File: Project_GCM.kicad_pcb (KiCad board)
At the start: 4 copper layers, 203 x 116 mm, 127 parts, among them J1 PowerSupply, J10 MM1_addressExtension, J11 MM1_receptacle_5530843-2, J12 DEBUG_BUSES, J13 MM1_addressExtension, J2 PP1_receptacle_TE_5-5530843-4, J3 PP1_receptacle_TE_5-5530843-4, J4 PP1_receptacle_TE_5-5530843-4, J5 PP1_receptacle_TE_5-5530843-4, J6 TE_Eurocard_96pole, J7 3-641124-6, J8 MM1_receptacle_5530843-2, J9 Conn_01x02, U1 LM810, U10 74LVC1G74, U11 74AHC1G04, U12 74AHC244, U13 CD74AC161M, U14 CD74AC161M, U15 74AHCT1G04, U16 CD74AC161M, U17 CD74AC161M, U18 74AHC1G04, U19 CD74AC161M, U2 LTC6994xS6-1, U20 CD74AC161M, U21 74AHCT244, U22 74CBTLV16212, U23 74CBTLV16212, U24 74CBTLV16212, U25 74AHC1G32, U26 SN74LV393A, U27 SN74LV393A, U28 CD74AC151, U29 CD74AC151, U3 74AHC1G32, U30 74AHC1G32, U31 CD74AC151, U32 74AHC273, U33 SN74LV393A, U34 SN74LV393A, U35 CD74AC151, U36 CD74AC151, U37 CD74AC151, U38 74AHC1G04, U39 74AHC1G04, U4 74AHC273, U40 74AHC273, U41 74AHC1G04, U42 74AHC273, U43 74AHC273, U44 74AHC273, U5 74AHC1G04, U6 CD74AC238, U7 74AHC138, U8 74AHC244, U9 74AHC244, X1 ECS-2200BX-500

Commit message: Netlist, apply change to board, clean track, #6 #4 #12 #10
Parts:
- removed C51: 10nF, Capacitor_SMD:C_0805_2012Metric
- removed G***: LOGO, QRCode:QRCode
- removed U38, U39: 74AHC1G04, Package_TO_SOT_SMD:SOT-23-5
- added C56: 1uF, Capacitor_SMD:C_0805_2012Metric, B.Cu at (258.0, 54.0)
- C11, C4: footprint Capacitor_SMD:C_1206_3216Metric -> Capacitor_SMD:C_0805_2012Metric
- C2: value 10nF -> 1uF
- C3, C5: value 10nF -> 100nF
- J12: footprint Connector_PinSocket_2.54mm:PinSocket_2x21_P2.54mm_Vertical -> Connector_PinHeader_2.54mm:PinHeader_2x21_P2.54mm_Vertical
- J7: footprint Connector_PinSocket_2.54mm:PinSocket_1x06_P2.54mm_Vertical -> TE_3-641124-6:TE_3-641124-6
- J9: footprint Connector_PinSocket_2.54mm:PinSocket_1x02_P2.54mm_Vertical -> Connector_PinHeader_2.54mm:PinHeader_1x02_P2.54mm_Vertical
- moved C14 14.9 mm to (144.0, 143.0)
- moved C2 14.8 mm to (263.0, 47.0), turned to 180 degrees
- moved C5 9.50 mm to (256.0, 54.0), turned to 90 degrees
- moved R5 7.02 mm to (143.0, 136.0)
- moved J7 7.00 mm to (139.0, 139.5), turned to 0 degrees
- moved C3 5.41 mm to (263.0, 45.0), turned to 180 degrees
- moved C15 3.04 mm to (253.0, 38.0)
- moved J12 2.31 mm to (198.1, 40.6)
- moved R4 1.12 mm to (190.5, 44.5)
- moved J9 1.08 mm to (190.5, 38.1)
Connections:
- C2 pad 1: +12V -> +5V
- U13 pad 2: /AddressCounter/ADDSRC_DELAYED_CLK -> /ADDSRC_CLK
- U14 pad 2: /AddressCounter/ADDSRC_DELAYED_CLK -> /ADDSRC_CLK
- U16 pad 2: /AddressCounter/ADDSRC_DELAYED_CLK -> /ADDSRC_CLK
- U17 pad 2: /AddressCounter/ADDSRC_DELAYED_CLK -> /ADDSRC_CLK
- U19 pad 2: /AddressCounter/ADDSRC_DELAYED_CLK -> /ADDSRC_CLK
- U20 pad 2: /AddressCounter/ADDSRC_DELAYED_CLK -> /ADDSRC_CLK
- U26 pad 3: /ClockGenerator/CLK_50d16MHZ -> /ClockGenerator/CLK_50d2MHZ
- U26 pad 4: /ClockGenerator/CLK_50d8MHZ -> /ClockGenerator/CLK_50d4MHZ
- U26 pad 5: /ClockGenerator/CLK_50d4MHZ -> /ClockGenerator/CLK_50d8MHZ
- U26 pad 6: /ClockGenerator/CLK_50d2MHZ -> /ClockGenerator/CLK_50d16MHZ
- U27 pad 3: /ClockGenerator/CLK_50d4096MHZ -> /ClockGenerator/CLK_50d512MHZ
- U27 pad 4: /ClockGenerator/CLK_50d2048MHZ -> /ClockGenerator/CLK_50d1024MHZ
- U27 pad 5: /ClockGenerator/CLK_50d1024MHZ -> /ClockGenerator/CLK_50d2048MHZ
- U27 pad 6: /ClockGenerator/CLK_50d512MHZ -> /ClockGenerator/CLK_50d4096MHZ
- U33 pad 3: /ClockGenerator/PClockGenerator/CLK_50d16MHZ -> /ClockGenerator/PClockGenerator/CLK_50d2MHZ
- U33 pad 4: /ClockGenerator/PClockGenerator/CLK_50d8MHZ -> /ClockGenerator/PClockGenerator/CLK_50d4MHZ
- U33 pad 5: /ClockGenerator/PClockGenerator/CLK_50d4MHZ -> /ClockGenerator/PClockGenerator/CLK_50d8MHZ
- U33 pad 6: /ClockGenerator/PClockGenerator/CLK_50d2MHZ -> /ClockGenerator/PClockGenerator/CLK_50d16MHZ
- U34 pad 3: /ClockGenerator/PClockGenerator/CLK_50d4096MHZ -> /ClockGenerator/PClockGenerator/CLK_50d512MHZ
- U34 pad 4: /ClockGenerator/PClockGenerator/CLK_50d2048MHZ -> /ClockGenerator/PClockGenerator/CLK_50d1024MHZ
- U34 pad 5: /ClockGenerator/PClockGenerator/CLK_50d1024MHZ -> /ClockGenerator/PClockGenerator/CLK_50d2048MHZ
- U34 pad 6: /ClockGenerator/PClockGenerator/CLK_50d512MHZ -> /ClockGenerator/PClockGenerator/CLK_50d4096MHZ
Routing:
- net GND: track 1447.7 -> 0.00 mm, vias 15 -> 0
- net +5V: track 790.6 -> 0.00 mm, vias 12 -> 0
- net +3V3: track 535.7 -> 0.00 mm, vias 7 -> 0
- net /ClockGenerator/BWRITE1_5: track 330.1 -> 0.00 mm, vias 5 -> 0
- net /ClockGenerator/BWRITE1_0: track 326.7 -> 0.00 mm, vias 6 -> 0
- net /ClockGenerator/BWRITE1_4: track 324.2 -> 0.00 mm, vias 5 -> 0
- net /ClockGenerator/BWRITE1_1: track 309.6 -> 0.00 mm, vias 4 -> 0
- net /ClockGenerator/BWRITE1_2: track 309.0 -> 0.00 mm, vias 4 -> 0
- net /Connector/BWRITE2_4: track 302.5 -> 0.00 mm, vias 4 -> 0
- net /ClockGenerator/BWRITE1_3: track 300.6 -> 0.00 mm, vias 5 -> 0
- net /Connector/BWRITE2_0: track 299.3 -> 0.00 mm, vias 5 -> 0
- net /Connector/BWRITE2_2: track 295.9 -> 0.00 mm, vias 4 -> 0
- net /Connector/BWRITE2_5: track 294.0 -> 0.00 mm, vias 5 -> 0
- net /Connector/BWRITE2_1: track 289.8 -> 0.00 mm, vias 3 -> 0
- net /Connector/BWRITE2_3: track 285.9 -> 0.00 mm, vias 3 -> 0
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
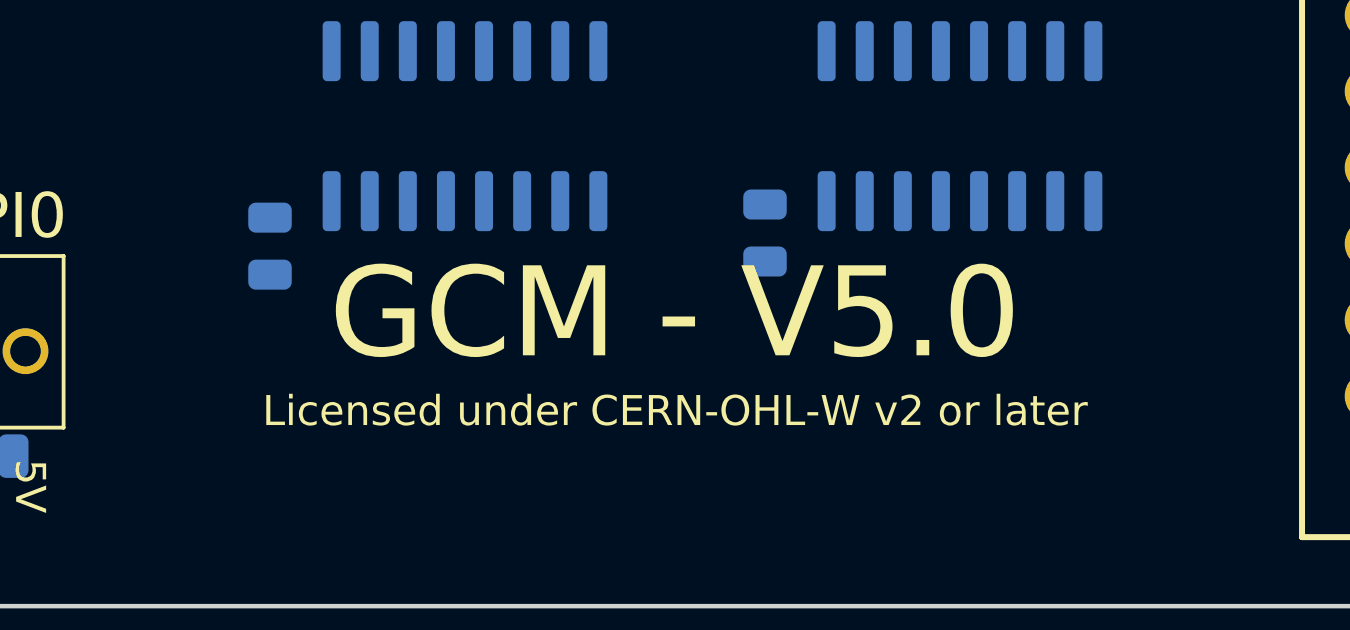
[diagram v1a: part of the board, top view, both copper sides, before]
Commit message: Set version to 5.1, 2021 copyright and date, replace the missing QRcode
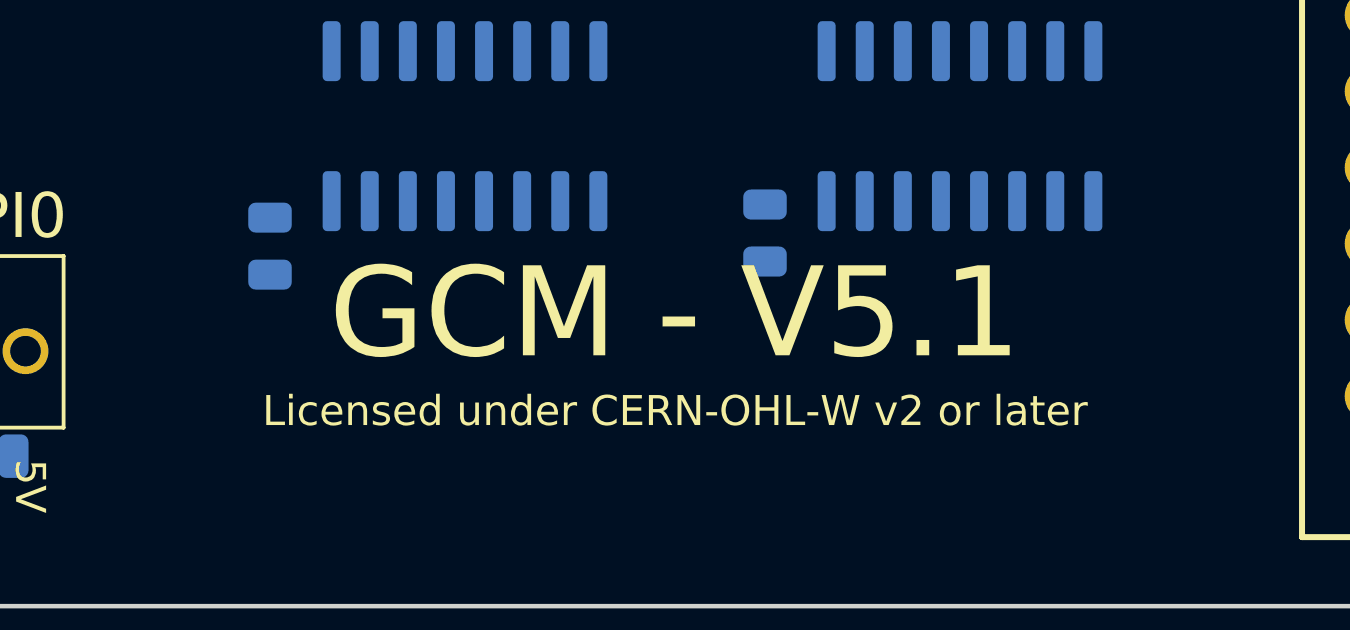
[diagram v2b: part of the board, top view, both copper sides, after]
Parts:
- added GQR1: LOGO, QRCode:QRCode, B.Cu at (249.0, 71.5)
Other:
- board text added: "GCM - V5.1"
- board text removed: "GCM - V5.0"

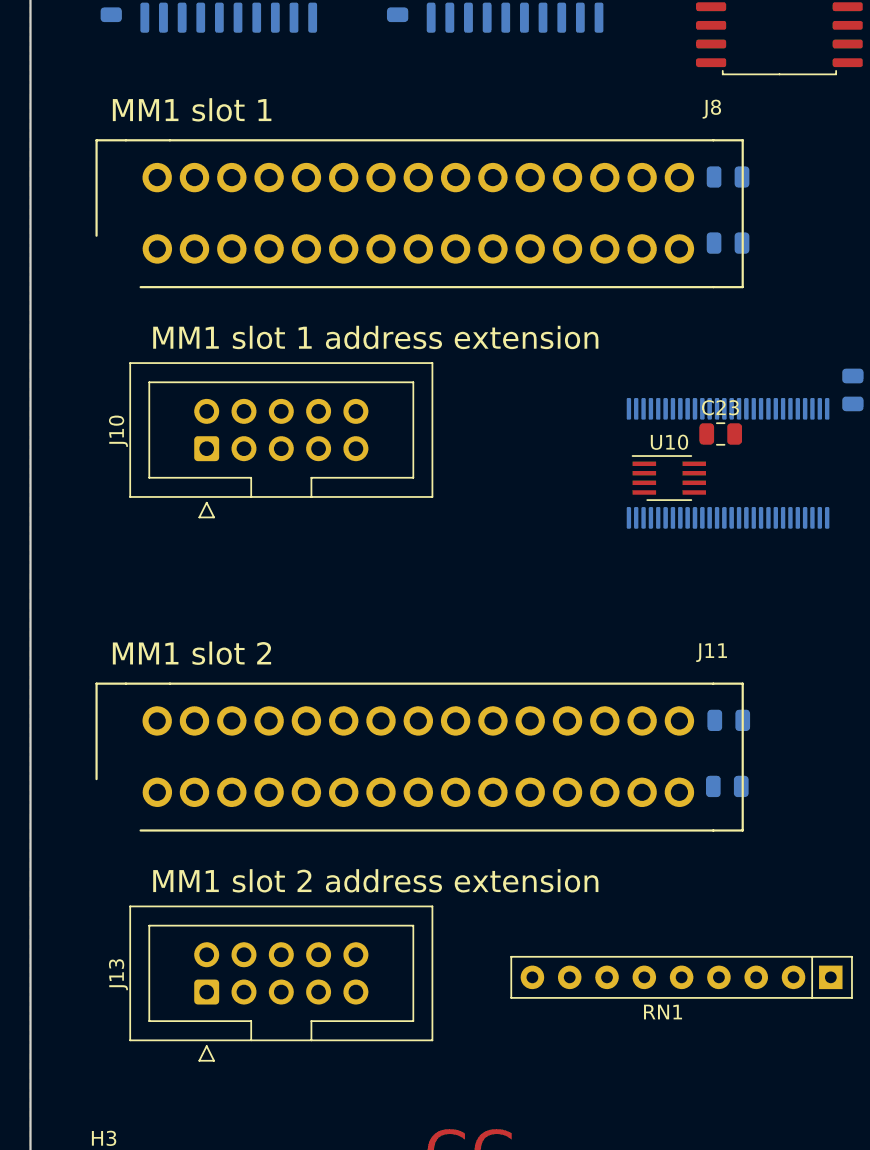
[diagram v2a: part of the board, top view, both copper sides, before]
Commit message: Back the MM1 connectors #8
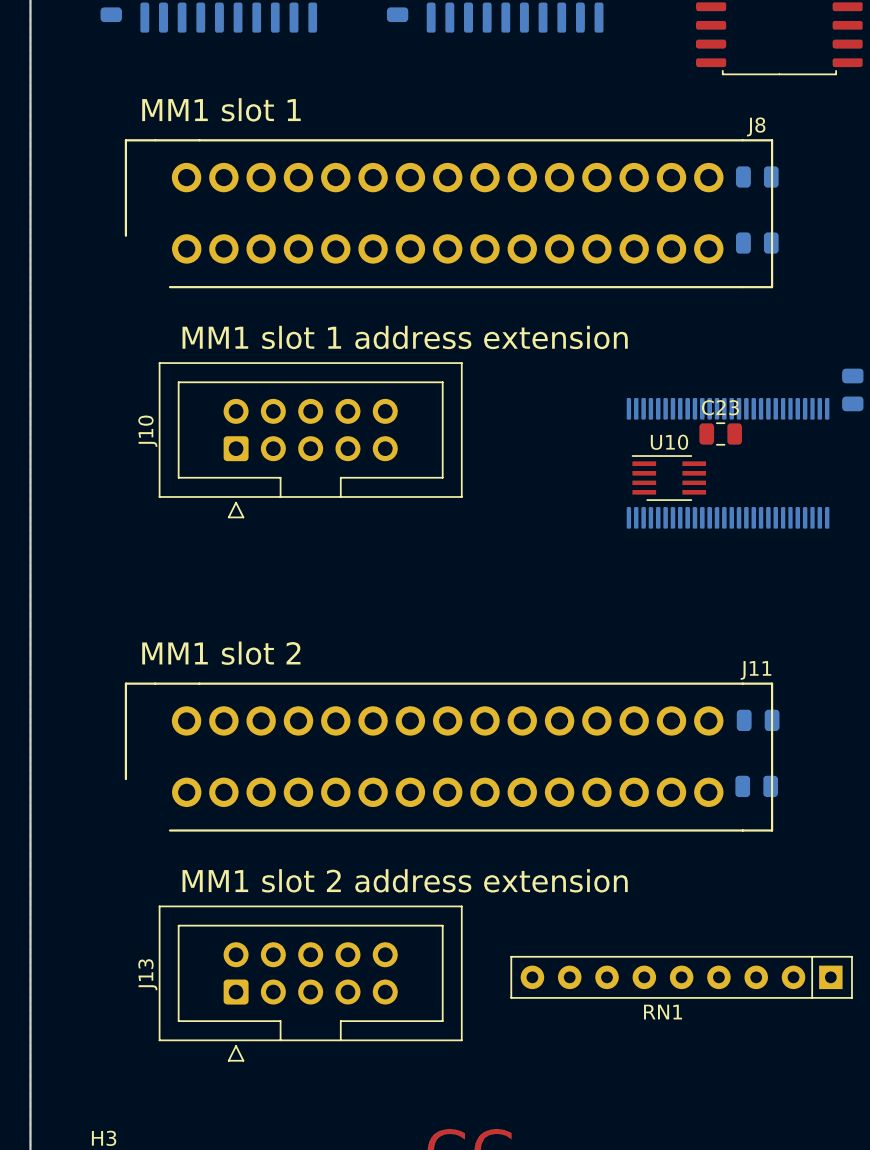
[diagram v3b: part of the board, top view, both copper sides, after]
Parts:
- moved C26 2.00 mm to (117.5, 78.0)
- moved C27 2.00 mm to (117.5, 73.5)
- moved C33 2.00 mm to (117.5, 115.0)
- moved C34 2.00 mm to (117.5, 110.5)
- moved J10 2.00 mm to (82.0, 92.0)
- moved J11 2.00 mm to (96.5, 113.0)
- moved J13 2.00 mm to (82.0, 129.0)
- moved J8 2.00 mm to (96.5, 76.0)

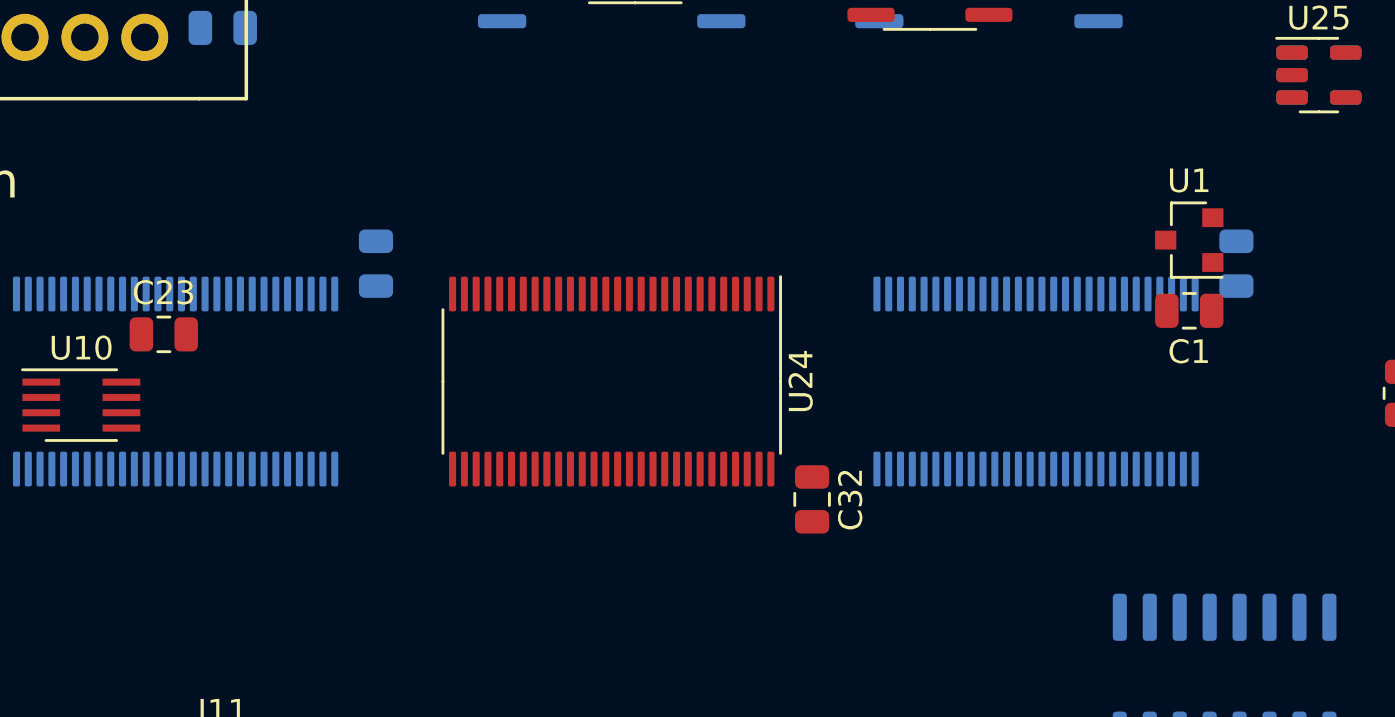
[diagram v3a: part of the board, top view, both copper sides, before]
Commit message: Replace capacitor for U22 U23 U24 #13
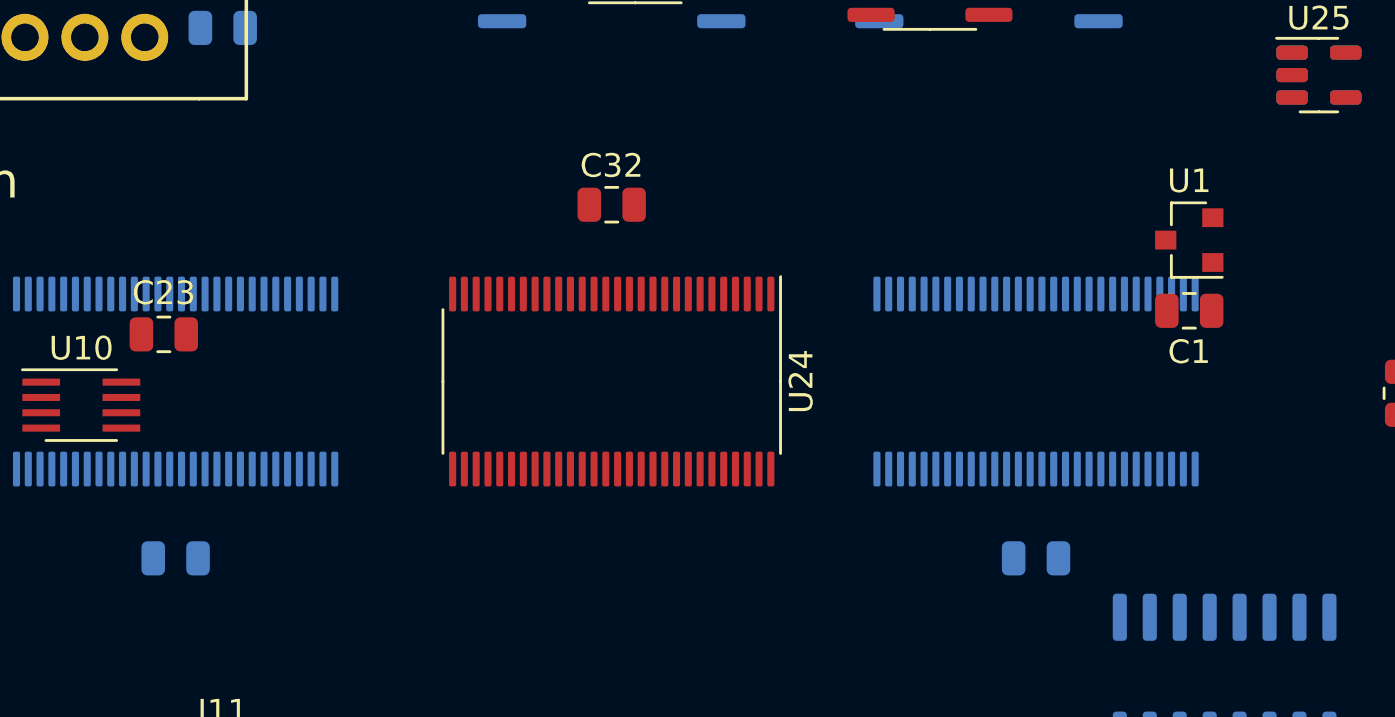
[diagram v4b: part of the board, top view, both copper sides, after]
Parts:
- moved C30 15.1 mm to (115.5, 100.5), turned to 0 degrees
- moved C31 15.1 mm to (152.0, 100.5), turned to 0 degrees
- moved C32 15.1 mm to (134.0, 85.5), turned to 0 degrees

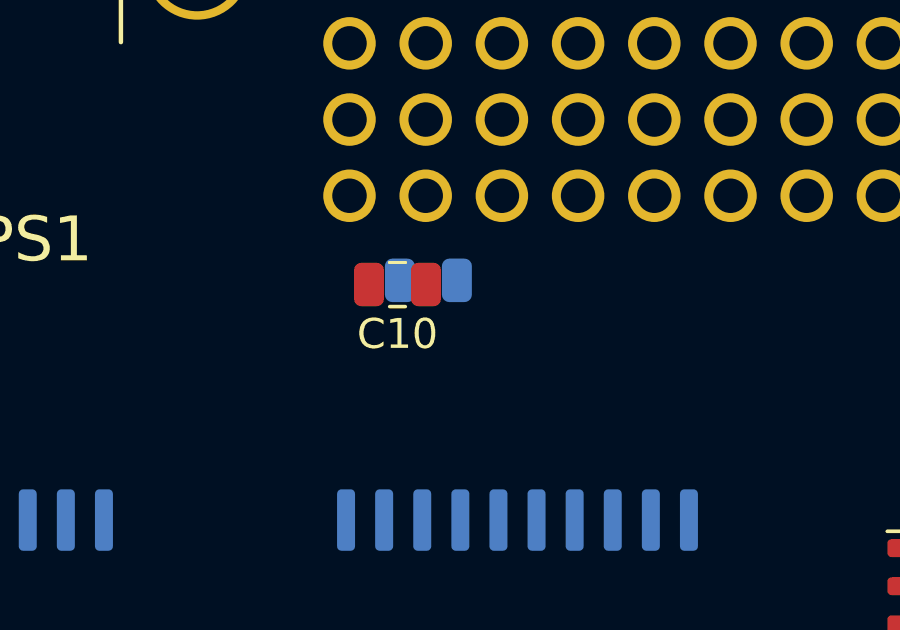
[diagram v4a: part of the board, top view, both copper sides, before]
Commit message: Better decoupling
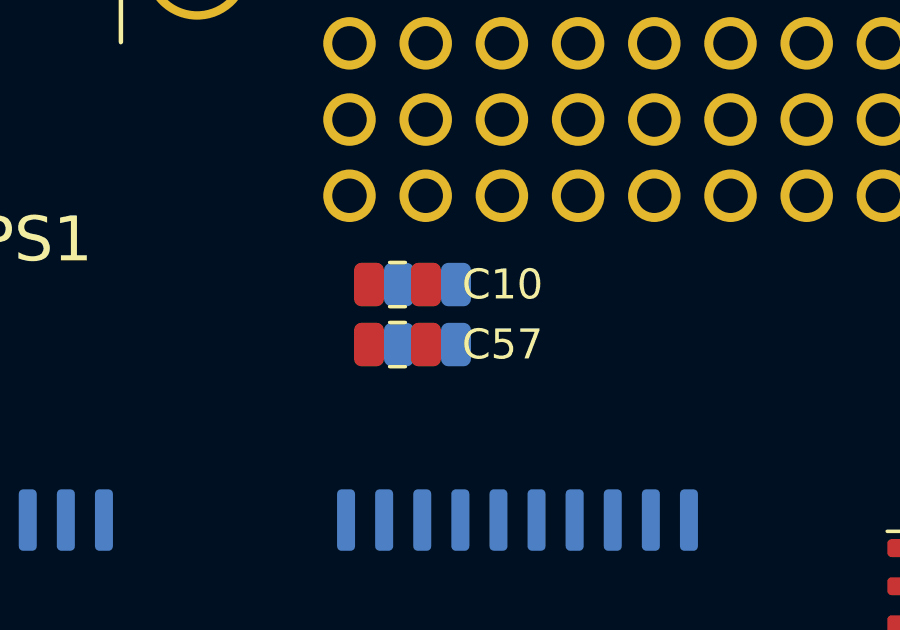
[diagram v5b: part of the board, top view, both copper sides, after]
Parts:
- added C51: 1uF, Capacitor_SMD:C_0805_2012Metric, B.Cu at (98.0, 47.5)
- added C57: 1uF, Capacitor_SMD:C_0805_2012Metric, F.Cu at (97.0, 47.5)
- C10, C14, C15, C25, C26, C27, C33, C34, C42, C43, C44, C45, C46, C47, C48, C9: value 10nF -> 100nF
- moved C9 0.14 mm to (98.0, 45.5)

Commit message: Precise the molex connector for power supply
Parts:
- J1: value PowerSupply -> Molex_1053102116

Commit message: First step, import ses
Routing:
- net GND: track 0.00 -> 1410.1 mm, vias 0 -> 14
- net +5V: track 0.00 -> 755.6 mm, vias 0 -> 7
- net +3V3: track 0.00 -> 540.7 mm, vias 0 -> 7
- net /ClockGenerator/BWRITE1_0: track 0.00 -> 328.9 mm, vias 0 -> 8
- net /ClockGenerator/BWRITE1_4: track 0.00 -> 322.5 mm, vias 0 -> 5
- net /ClockGenerator/BWRITE1_5: track 0.00 -> 311.1 mm, vias 0 -> 6
- net /ClockGenerator/BWRITE1_1: track 0.00 -> 298.9 mm, vias 0 -> 6
- net /ClockGenerator/BWRITE1_2: track 0.00 -> 297.6 mm, vias 0 -> 5
- net /Connector/BWRITE2_0: track 0.00 -> 291.3 mm, vias 0 -> 3
- net /Connector/BWRITE2_2: track 0.00 -> 288.6 mm, vias 0 -> 4
- net /ClockGenerator/BWRITE1_3: track 0.00 -> 288.3 mm, vias 0 -> 5
- net /Connector/BWRITE2_4: track 0.00 -> 284.5 mm, vias 0 -> 5
- net /Connector/BWRITE2_6: track 0.00 -> 282.0 mm, vias 0 -> 2
- net /Connector/BWRITE2_1: track 0.00 -> 278.8 mm, vias 0 -> 3
- net /Connector/BWRITE2_3: track 0.00 -> 276.9 mm, vias 0 -> 4
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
